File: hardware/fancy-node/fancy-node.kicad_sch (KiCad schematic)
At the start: 55 parts, among them J1 Conn_01x05, J2 Conn_01x03, J3 Conn_01x04, J4 USB_B_Micro, U5 HT75xx-1-SOT89, U6 RFM69CW-915MHZ, U7 TP4056

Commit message: Schematic and placement for fancy-node
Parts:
- removed C?: 10uF, Capacitor_SMD:C_0603_1608Metric, symbol Device:C
- removed C?: 100nF, Capacitor_SMD:C_0402_1005Metric_Pad0.74x0.62mm_HandSolder, symbol Device:C
- removed H4: MountingHole, MountingHole:MountingHole_3.2mm_M3, symbol Mechanical:MountingHole
- removed J1: Conn_01x05, Connector_PinHeader_2.54mm:PinHeader_1x05_P2.54mm_Vertical, symbol Connector_Generic:Conn_01x05
- removed J2: Conn_01x03, Connector_PinHeader_2.54mm:PinHeader_1x03_P2.54mm_Horizontal, symbol Connector_Generic:Conn_01x03
- removed R?: 1k, Resistor_SMD:R_0603_1608Metric, symbol Device:R
- added H5: StrainRelief, Homebrew:3_pin_2.54mm_pitch_strain_relief, symbol Mechanical:MountingHole
- added J1: Conn_01x06, Connector_PinHeader_2.54mm:PinHeader_1x06_P2.54mm_Vertical, symbol Connector_Generic:Conn_01x06
- added J2: Conn_01x02, Connector_JST:JST_GH_SM02B-GHS-TB_1x02-1MP_P1.25mm_Horizontal, symbol Connector_Generic:Conn_01x02
- added J5: Conn_01x03, Connector_PinHeader_2.54mm:PinHeader_1x03_P2.54mm_Horizontal, symbol Connector_Generic:Conn_01x03
- added R3: 3k3, Resistor_SMD:R_0603_1608Metric, symbol Device:R
- added R5: 1k, Resistor_SMD:R_0402_1005Metric, symbol Device:R
- added SW4: SW_Push, Homebrew:SW_TACTILE_5.1MM_TS-1187A-C-D-B, symbol Switch:SW_Push
- J4: footprint homebrew:FRAMATOME_10118194-0001LF_fixed_bridges -> Homebrew:FRAMATOME_10118194-0001LF_fixed_bridges
- R1, R2: renamed from R?; footprint Resistor_SMD:R_0603_1608Metric -> Resistor_SMD:R_0402_1005Metric; LCSC C21190 -> C11702
- R31, R32: footprint Resistor_SMD:R_0603_1608Metric -> Resistor_SMD:R_0402_1005Metric; LCSC C21190 -> C11702
- R4: renamed from R?; footprint Resistor_SMD:R_0603_1608Metric -> Resistor_SMD:R_0402_1005Metric; LCSC C23140 -> C25105
- SW3: renamed from SW?; footprint (none) -> Homebrew:SK22D15L5_SP
- U3: renamed from U?; footprint (none) -> LED_SMD:LED_WS2812B_PLCC4_5.0x5.0mm_P3.2mm; LCSC (none) -> C2874885
- U6: footprint homebrew:RFM69CW-minimalpads -> Homebrew:RFM69CW-minimalpads
- U7: footprint snapeda:SOP127P600X175-9N -> Homebrew:SOP-8_3.9x4.9mm_P1.27mm_Thermal
- gave numbers to parts that had none: 13
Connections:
- net +BATT: now also C18.2, SW3.3 (C), J1.3 (Pin_3), J5.3 (Pin_3); no longer SW3.1 (A)
- net AUX0: now also U2.29 (PA9), J1.4 (Pin_4)
- net AUX1: now also U2.32 (PA10), J1.5 (Pin_5)
- net BATT_DIRECT: no longer C18.2
- net BOOT0: now also R3.1
- net EXTERNAL_LED: now also J5.2 (Pin_2)
- net GND: now also SW1.2, J1.1 (Pin_1), J2.1 (Pin_1), J5.1 (Pin_1), SW4.2; no longer R2.2
- net VBUS: now also R3.2
- net VCC: now also J1.2 (Pin_2)
- net at TH1.2: now also J2.2 (Pin_2)
- net at U2.20 (PB1): now also R2.1; no longer SW1.1
- net at U2.21 (PB2): now also R5.1
- net AUX2: now reaches U2.33 (PA11)
- net AUX2: now also J1.6 (Pin_6)
- new net: R2.2, SW1.1
- new net: R5.2, SW4.1
- no-connect marks 18 -> 44
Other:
- moved on the sheet: D1, R1, R2, SW1

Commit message: fancy-node v1.0
Change-Id: I2dc287329bd6c7a9f578761cfc67db086f282b4b
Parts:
- removed J2: Conn_01x02, Connector_JST:JST_GH_SM02B-GHS-TB_1x02-1MP_P1.25mm_Horizontal, symbol Connector_Generic:Conn_01x02
- added J2: Conn_01x03, Homebrew:MiniPV_78208-X03XXX_1x03_P2.54mm_Polarized_Horizontal, symbol Connector_Generic:Conn_01x03
- added R6, R7, R8: 1k, Resistor_SMD:R_0402_1005Metric, symbol Device:R
- SW3: LCSC (none) -> C2884795
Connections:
- net AUX0: now also U2.45 (PB6), R6.1; no longer J1.4 (Pin_4), U2.29 (PA9)
- net AUX1: now also U2.46 (PB7), R7.1; no longer J1.5 (Pin_5), U2.32 (PA10)
- net AUX2: now also R8.1; no longer J1.6 (Pin_6)
- net GND: now also J2.2 (Pin_2)
- net at TH1.2: now also J2.1 (Pin_1)
- new net: J1.5 (Pin_5), R7.2
- new net: J1.6 (Pin_6), R8.2
- new net: J1.4 (Pin_4), R6.2
- no-connect marks 44 -> 45
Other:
- moved on the sheet: D1, J1, R1, R2, R5, SW1, SW4

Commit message: fancy-node v1.1:
- Actually connect VBATT_DIV to micro
- Add resistor on DIO0 line to protect against firmware errors
- Move WS2812b line to SPI2, to not conflict with the radio SPI in case
we want to use the SPI with DMA to output the NRZ
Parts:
- added R4: 1k, Resistor_SMD:R_0402_1005Metric, symbol Device:R
- renumbered C3 to C1, C9 to C10, C12 to C11, C14 to C12, C25 to C13, C10 to C14, C19 to C17, C17 to C18, C4 to C2, C6 to C3, C7 to C4, C1 to C5, C18 to C6, C8 to C7, C11 to C8, C13 to C9, D26 to D3, D30 to D4, D31 to D5, D35 to D6, D39 to D7, H5 to H1, H1 to H2, H2 to H3, H3 to H4, J4 to J1, J1 to J2, J5 to J3, J2 to J4, J3 to J5, R29 to R10, R30 to R11, R31 to R12, R32 to R13, R33 to R14, R5 to R3, R6 to R5, R7 to R6, R8 to R7, R3 to R8, R4 to R9, SW4 to SW2, SW2 to SW3, SW3 to SW4, U5 to U4, U6 to U5, U7 to U6
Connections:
- net DIO0: now also R4.1; no longer U2.28 (PA8)
- net INTERNAL_LED: now also U2.32 (PA10); no longer U2.34 (PA12)
- net VBATT_DIV: now also U2.11 (PA0)
- new net: R4.2, U2.28 (PA8)
- no-connect marks 45 -> 44

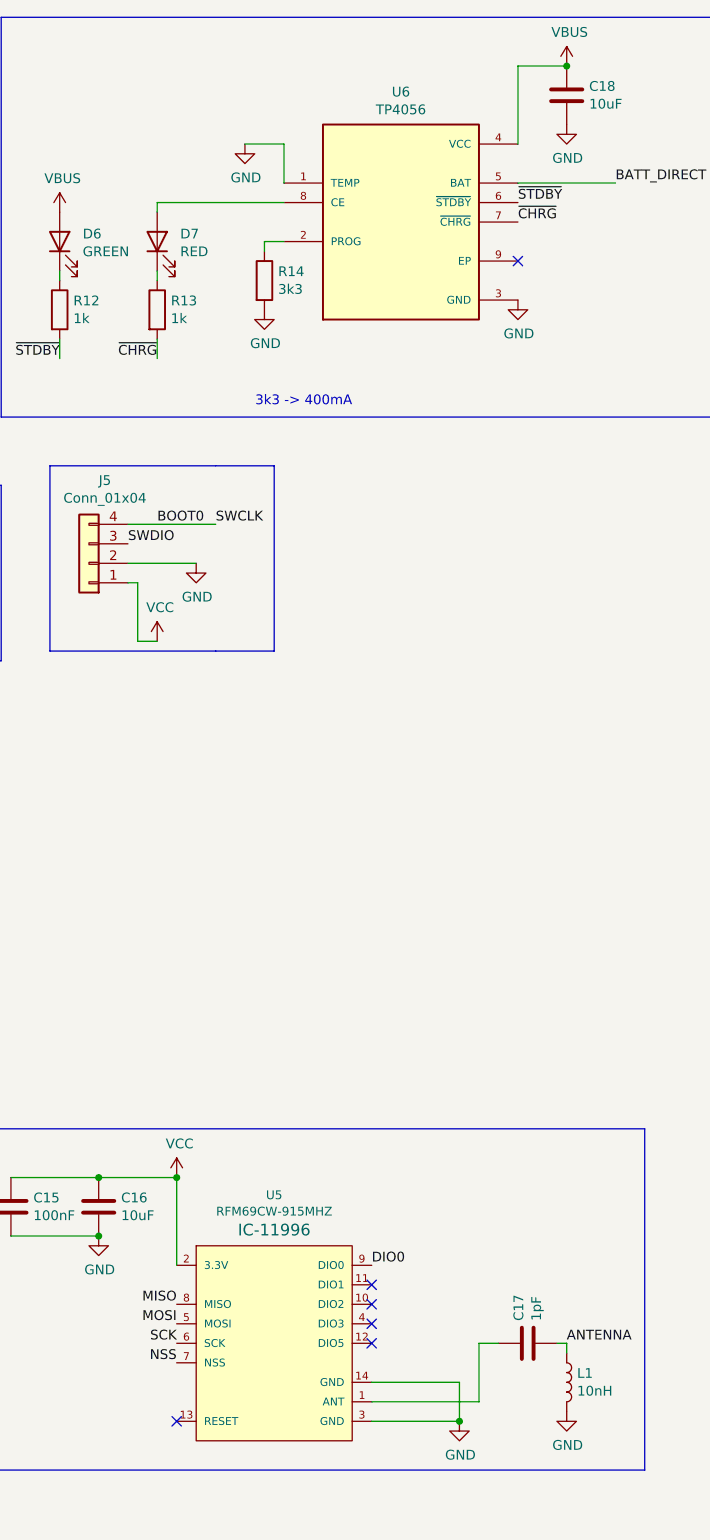
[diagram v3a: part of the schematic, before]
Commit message: Update fancy-node to KiCAD v7 and fix charging LED
Change-Id: Ied49e9baaabda8f003e0aa37fa23de49f58afb45
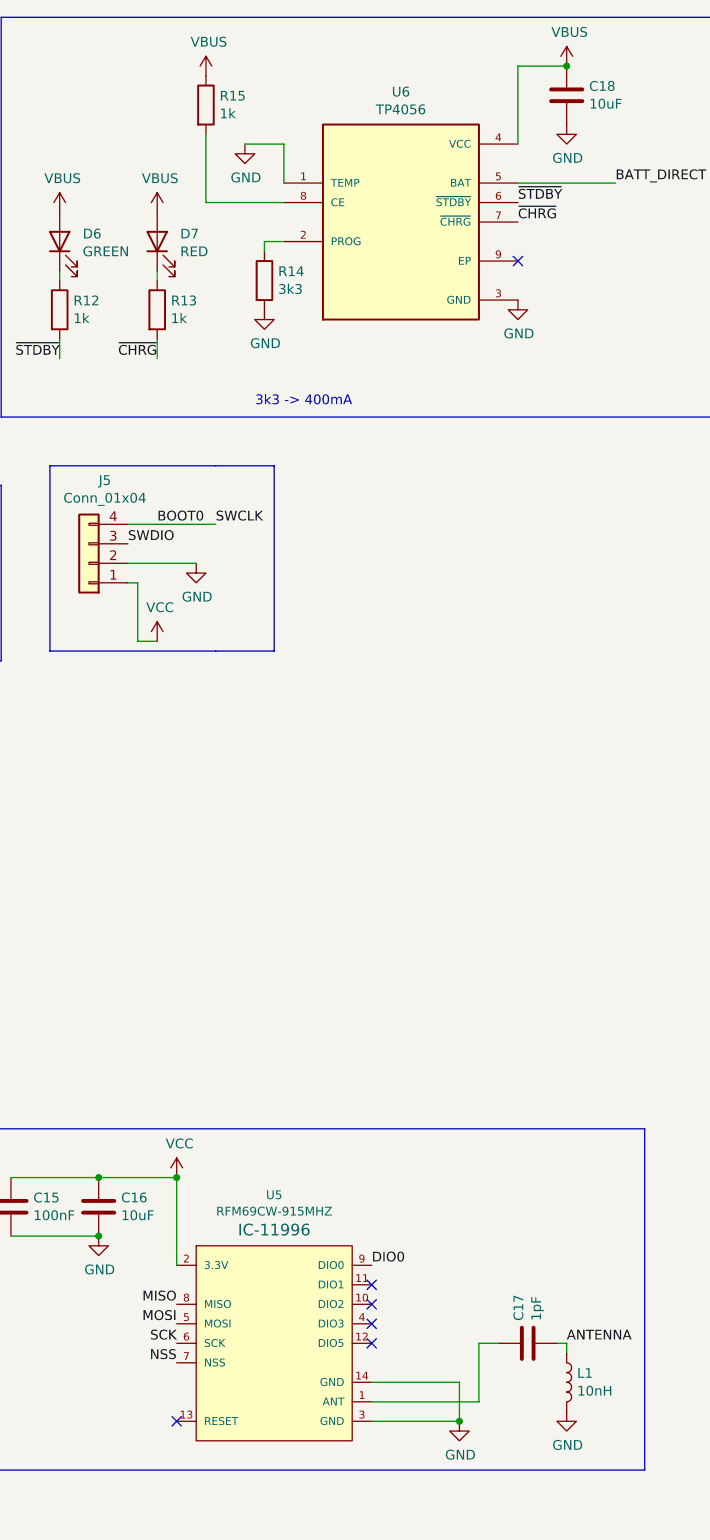
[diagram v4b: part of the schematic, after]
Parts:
- added R15: 1k, Resistor_SMD:R_0402_1005Metric, symbol Device:R
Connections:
- net VBUS: now also D7.2 (A), R15.1
- net at U6.8 (CE): now also R15.2; no longer D7.2 (A)

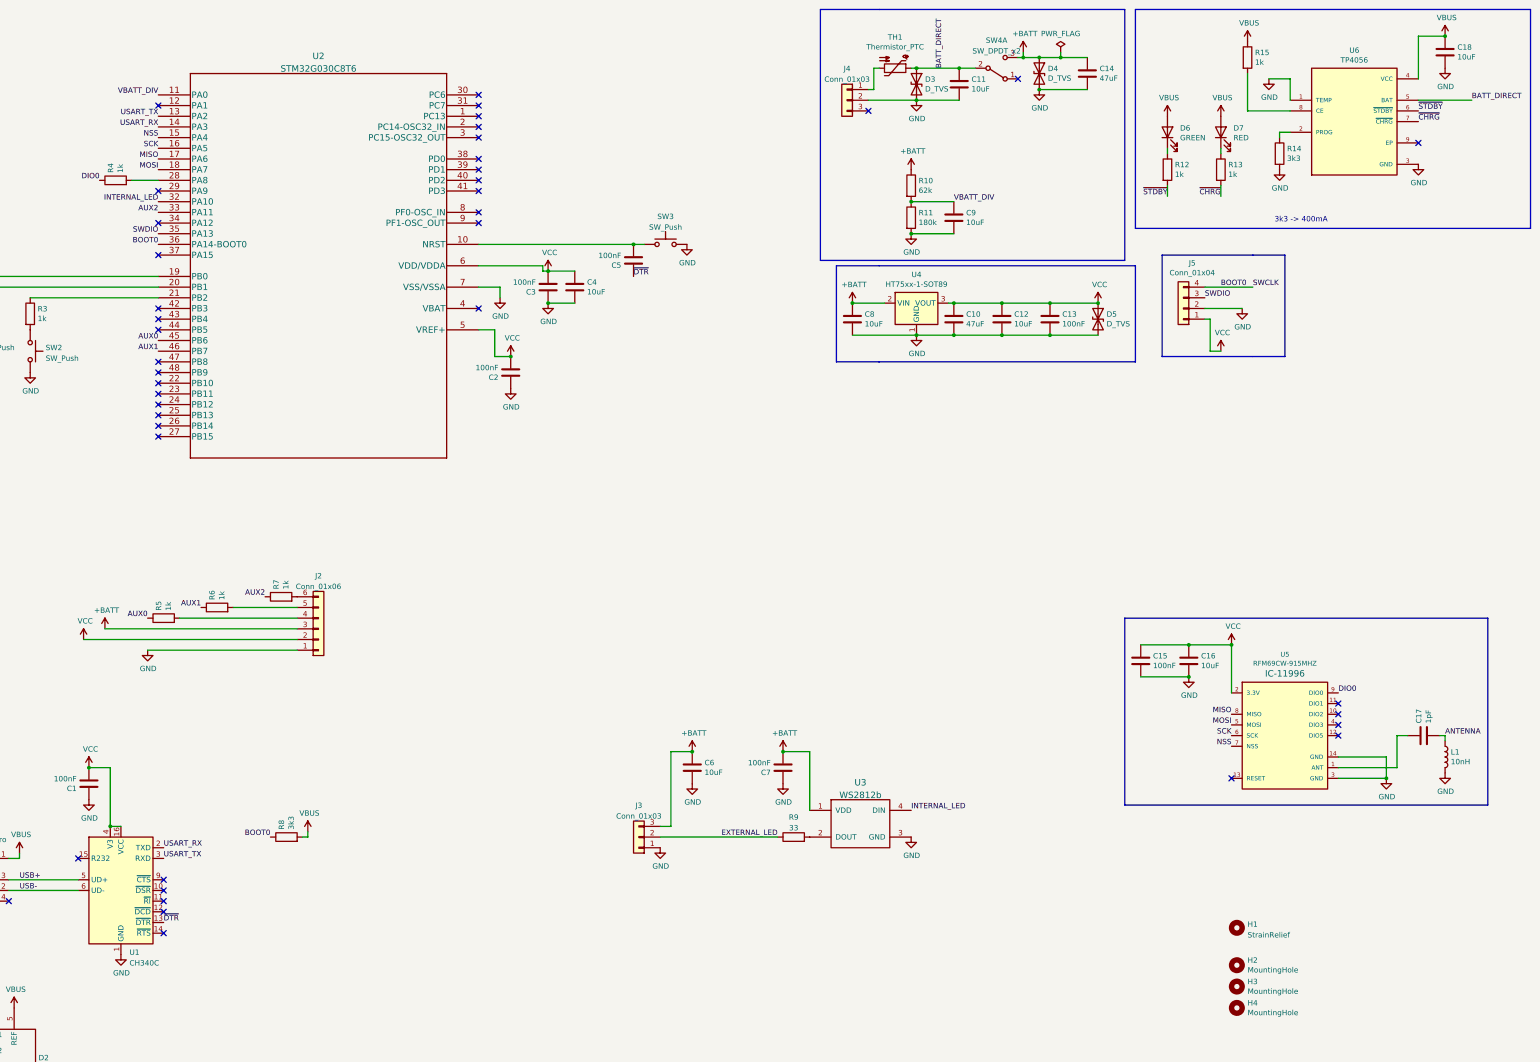
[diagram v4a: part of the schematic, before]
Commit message: Update schematic for fancy-node v1.2, and first pass at layout:
- Smaller buttons
- Smaller PCB antenna
- Smaller power switch
- Move to CH340X, hook up BOOT0 to it
- Smaller overall board size (47mm x 33mm, vs 60mm x 37mm)
- Add JST 1.25 for batteries
- Add crowbar diode for reverse polarity protection

Change-Id: I9a7a19972de9e62944e1a6f148661a5dd9e6b807
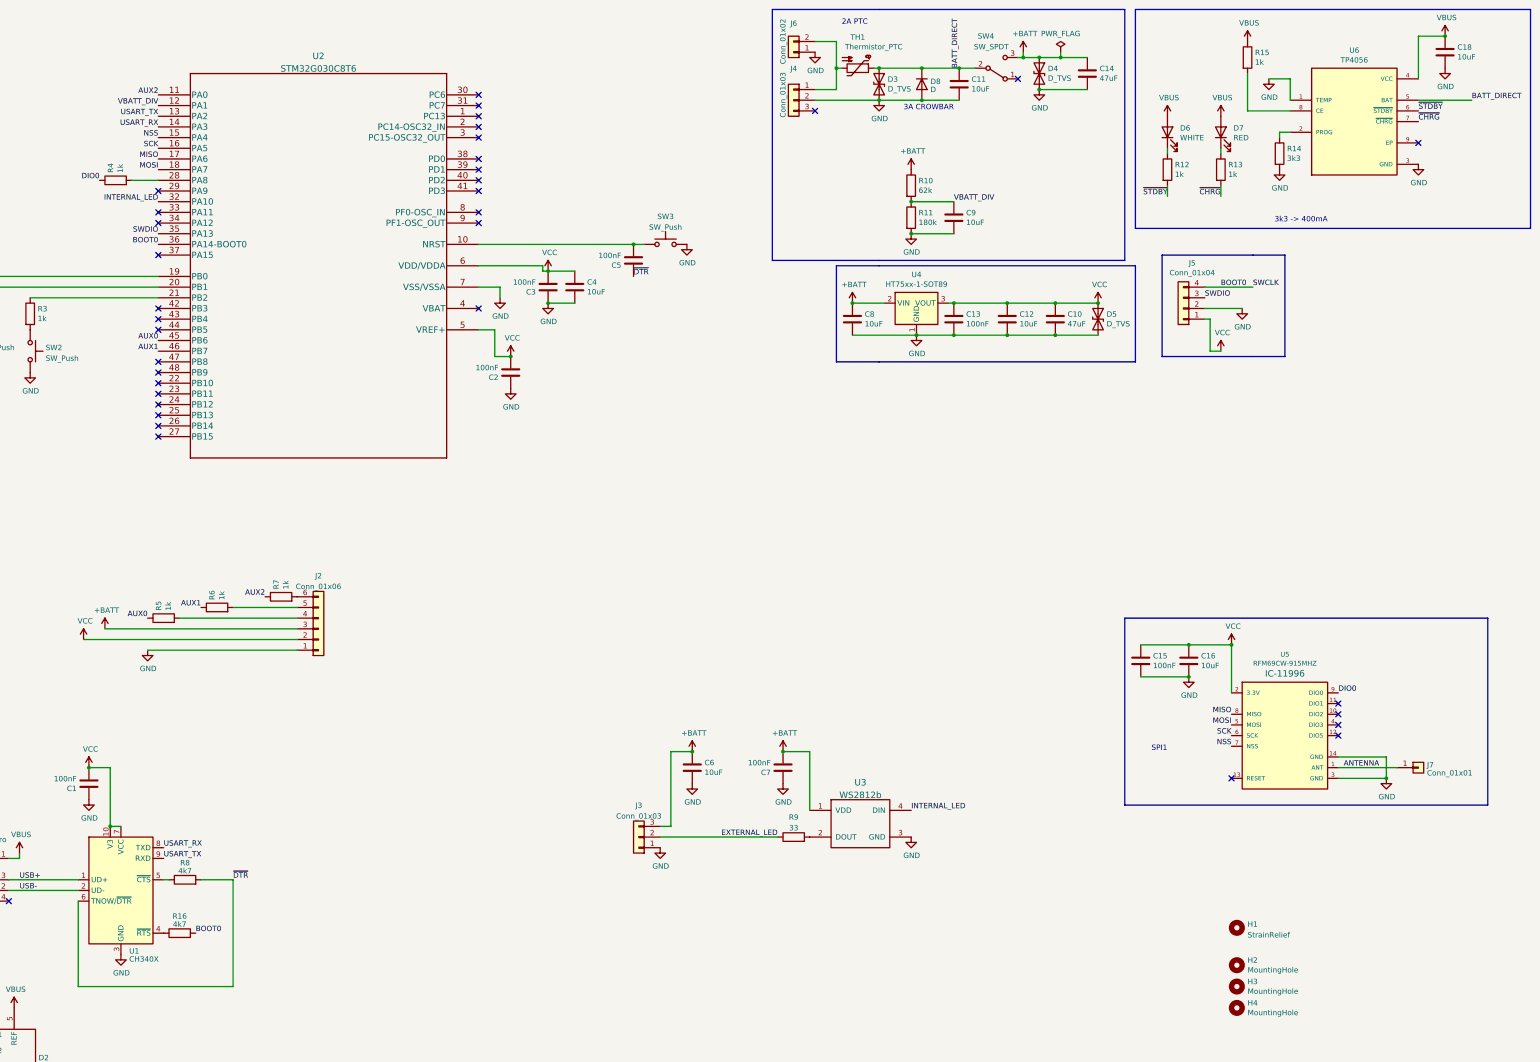
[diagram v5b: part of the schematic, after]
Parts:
- removed C17: 1pF, Capacitor_SMD:C_0402_1005Metric_Pad0.74x0.62mm_HandSolder, symbol Device:C
- removed L1: 10nH, Inductor_SMD:L_0402_1005Metric, symbol Device:L
- removed SW4: SW_DPDT_x2, Homebrew:SK22D15L5_SP, symbol Switch:SW_DPDT_x2
- removed U1: CH340C, Package_SO:SOIC-16_3.9x9.9mm_P1.27mm, symbol Interface_USB:CH340C
- added D8: D, Diode_SMD:D_SMA, symbol Device:D
- added J6: Conn_01x02, Homebrew:JST_Micro_1x02_P1.25mm_Horizontal, symbol Connector_Generic:Conn_01x02
- added J7: Conn_01x01, Connector_PinHeader_2.54mm:PinHeader_1x01_P2.54mm_Vertical, symbol Connector_Generic:Conn_01x01
- added R16: 4k7, Resistor_SMD:R_0402_1005Metric, symbol Device:R
- added SW4: SW_SPDT, Homebrew:SW_SLIDE_SPDT_K3-1204D-L, symbol Switch:SW_SPDT
- added U1: CH340X, Package_SO:MSOP-10_3x3mm_P0.5mm, symbol Interface_USB:CH340X
- D6: value GREEN -> WHITE; LCSC (none) -> C2290; MPN LTST-C190KGKT -> (none)
- R8: value 3k3 -> 4k7; footprint Resistor_SMD:R_0603_1608Metric -> Resistor_SMD:R_0402_1005Metric; LCSC C22978 -> C25900
- SW1, SW2, SW3: footprint Homebrew:SW_TACTILE_5.1MM_TS-1187A-C-D-B -> Homebrew:SW_TACTILE_3mmx3.5mm_TS-1071SA-A4B3-D4
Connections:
- net +BATT: now also SW4.3 (C)
- net ANTENNA: now also U5.1 (ANT), J7.1 (Pin_1)
- net AUX2: now also U2.11 (PA0); no longer U2.33 (PA11)
- net BATT_DIRECT: now also D8.1 (K), SW4.2 (B)
- net BOOT0: now also R16.2; no longer R8.1
- net GND: now also D8.2 (A), J6.1 (Pin_1), U1.3 (GND)
- net USART_RX: now also U1.8 (TXD)
- net USART_TX: now also U1.9 (RXD)
- net USB+: now also U1.1 (UD+)
- net USB-: now also U1.2 (UD-)
- net VBATT_DIV: now also U2.12 (PA1); no longer U2.11 (PA0)
- net VBUS: no longer R8.2
- net VCC: now also U1.10 (V3), U1.7 (VCC)
- net ~{DTR}: now also R8.2, U1.6 (TNOW/~{DTR})
- net at J4.1 (Pin_1), TH1.2: now also J6.2 (Pin_2)
- new net: R16.1, U1.4 (~{RTS})
- new net: R8.1, U1.5 (~{CTS})
- no-connect marks 44 -> 38
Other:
- note added: "2A PTC"
- note added: "3A CROWBAR"
- note added: "SPI1"
- moved on the sheet: C10, C12, C13, D3, J4, TH1

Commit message: More fancy-node v1.2 changes
Change-Id: I98cb262bb1c5ca5a4a3b6f15447a12dbf8e0580a
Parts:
- removed J7: Conn_01x01, Connector_PinHeader_2.54mm:PinHeader_1x01_P2.54mm_Vertical, symbol Connector_Generic:Conn_01x01
- added L1: 27nH, Inductor_SMD:L_0402_1005Metric, symbol Device:L
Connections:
- net ANTENNA: now also L1.2; no longer U5.1 (ANT)
- new net: L1.1, U5.1 (ANT)
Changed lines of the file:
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@@
     (effects (font (size 1.27 1.27)) (justify right bottom))
   )
-  (label "ANTENNA" (at 355.6 194.31 0) (fields_autoplaced)
+  (label "ANTENNA" (at 375.92 194.31 0) (fields_autoplaced)
     (effects (font (size 1.27 1.27)) (justify left bottom))
   )
@@
     )
   )
+  (symbol (lib_id "Device:L") (at 372.11 194.31 90) (unit 1)
+    (in_bom yes) (on_board yes) (dnp no) (fields_autoplaced)
+    (property "Reference" "L1" (at 372.11 190.7947 90)
+      (effects (font (size 1.27 1.27)))
+    )
+    (property "Value" "27nH" (at 372.11 192.7157 90)
+      (effects (font (size 1.27 1.27)))
+    )
+    (property "Footprint" "Inductor_SMD:L_0402_1005Metric" (at 372.11 194.31 0)
+      (effects (font (size 1.27 1.27)) hide)
+    )
+    (property "Datasheet" "~" (at 372.11 194.31 0)
+      (effects (font (size 1.27 1.27)) hide)
+    )
+    (property "LCSC" "C2041663" (at 372.11 194.31 90)
+      (effects (font (size 1.27 1.27)) hide)
+    )
+    (pin "1")
+    (pin "2")
+    (instances
+      (project "fancy-node"
+        (path "/e443e095-f4ba-4771-8554-3425f127ef3e"
+          (reference "L1") (unit 1)
+        )
+      )
+    )
+  )
   (symbol (lib_id "power:GND") (at 157.48 104.14 0) (unit 1)
     (in_bom yes) (on_board yes) (dnp no)
@@
         )
       )
-    )
-  )
-  (symbol (lib_id "Connector_Generic:Conn_01x01") (at 373.38 194.31 0) (unit 1)
-    (in_bom yes) (on_board yes) (dnp no) (fields_autoplaced)
-    (property "Reference" "J7" (at 375.412 193.6663 0)
-      (effects (font (size 1.27 1.27)) (justify left))
-    )
-    (property "Value" "Conn_01x01" (at 375.412 195.5873 0)
-      (effects (font (size 1.27 1.27)) (justify left))
-    )
-    (property "Footprint" "Connector_PinHeader_2.54mm:PinHeader_1x01_P2.54mm_Vertical" (at 373.38 194.31 0)
-      (effects (font (size 1.27 1.27)) hide)
-    )
-    (property "Datasheet" "~" (at 373.38 194.31 0)
-      (effects (font (size 1.27 1.27)) hide)
-    )
-    (pin "1")
-    (instances
-      (project "fancy-node"
-        (path "/e443e095-f4ba-4771-8554-3425f127ef3e"
-          (reference "J7") (unit 1)
-        )
-      )
